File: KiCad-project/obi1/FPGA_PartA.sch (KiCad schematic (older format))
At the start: 14 parts, among them SW1 SW_Push, U3 XC6SLX16-FTG256, U4 OSC

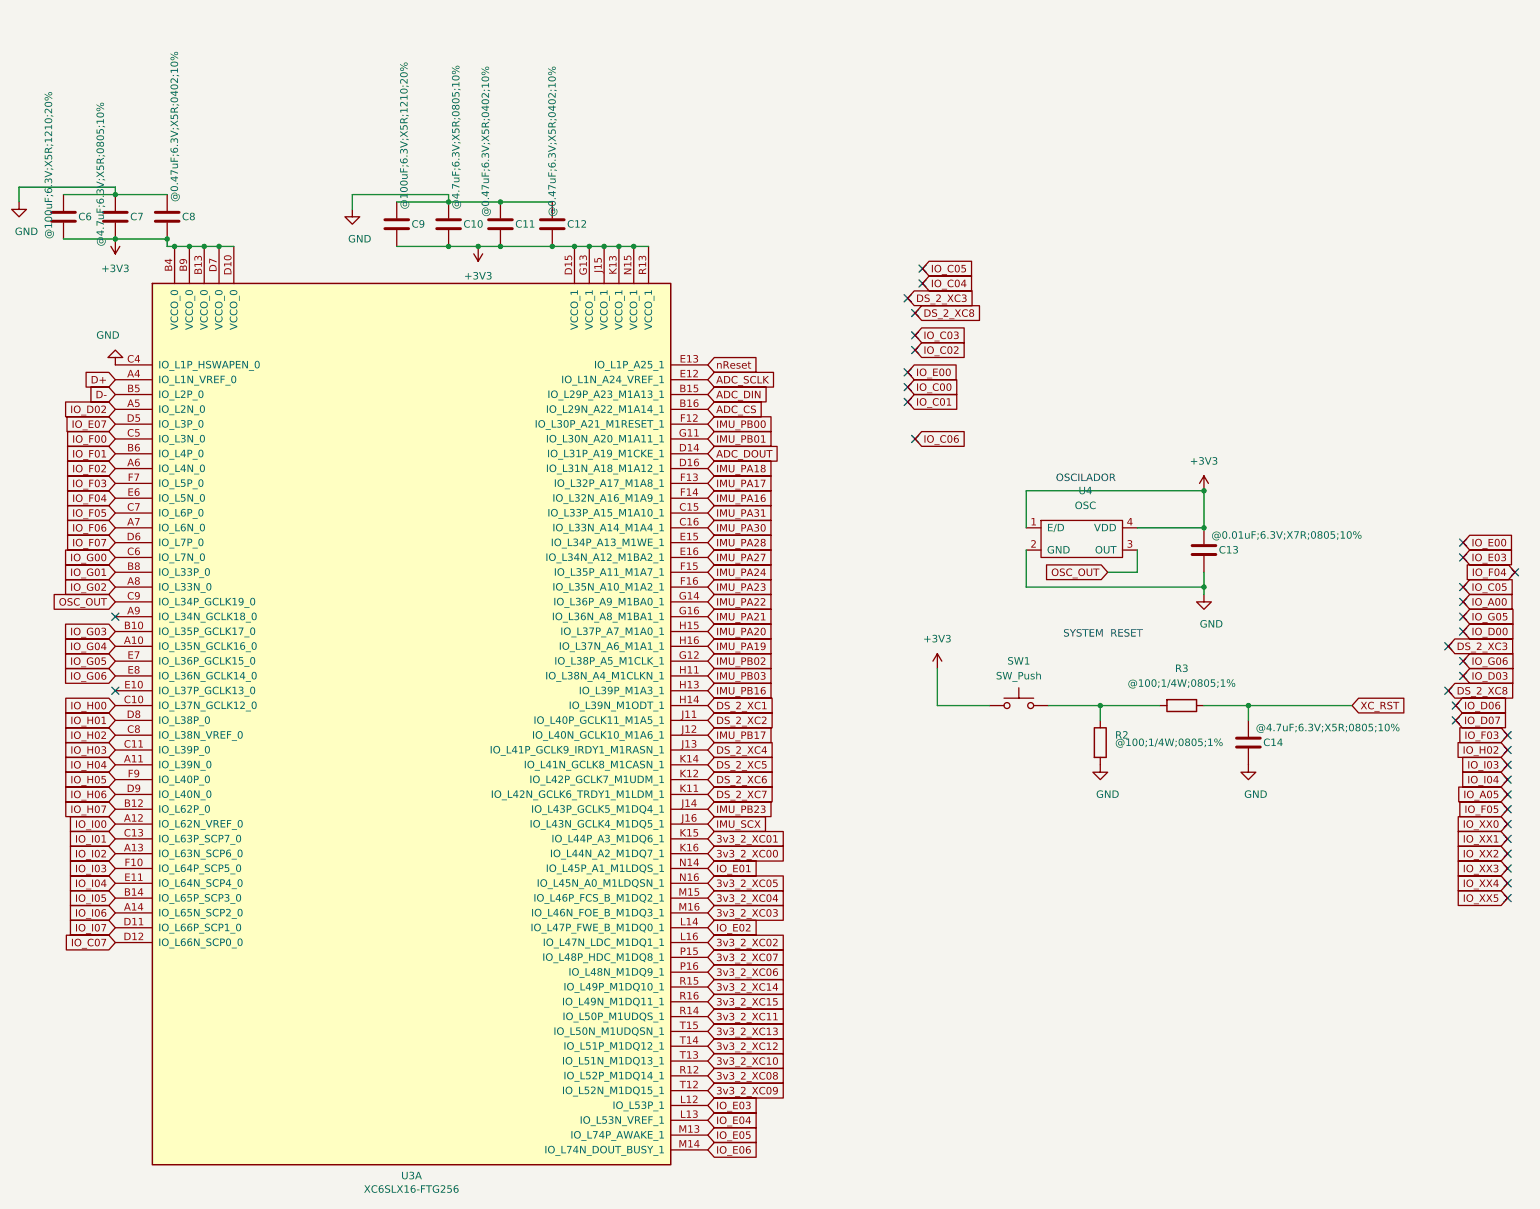
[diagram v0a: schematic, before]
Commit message: Resize board, change layout, re-route IO pins, new imu added
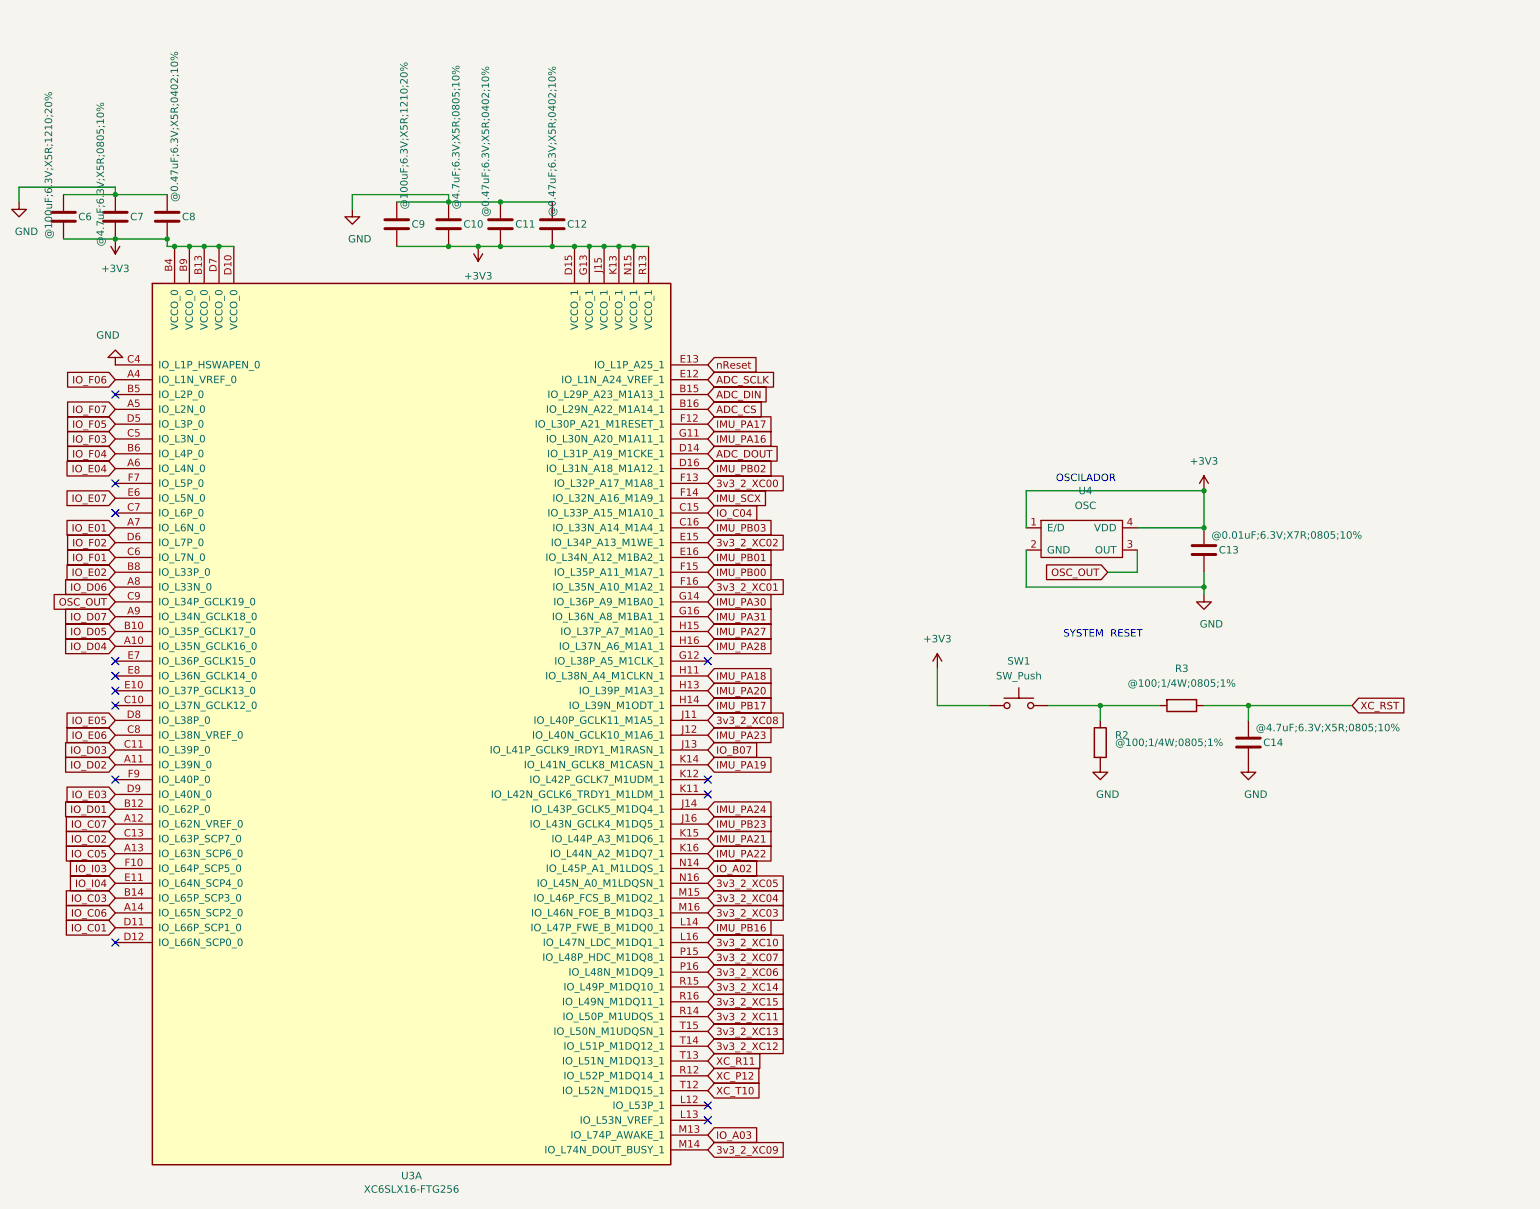
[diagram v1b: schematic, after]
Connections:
- net D+ is gone; now on net IO_F06: U3.A4 (IO_L1N_VREF_0)
- net DS_2_XC1 is gone; now on net IMU_PB17: U3.H14 (IO_L39N_M1ODT_1)
- net DS_2_XC2 is gone; now on net 3v3_2_XC08: U3.J11 (IO_L40P_GCLK11_M1A5_1)
- net DS_2_XC5 is gone; now on net IMU_PA19: U3.K14 (IO_L41N_GCLK8_M1CASN_1)
- net IO_F00 is gone; now on net IO_F03: U3.C5 (IO_L3N_0)
- net IO_G00 is gone; now on net IO_F01: U3.C6 (IO_L7N_0)
- net IO_G01 is gone; now on net IO_E02: U3.B8 (IO_L33P_0)
- net IO_G02 is gone; now on net IO_D06: U3.A8 (IO_L33N_0)
- net IO_H01 is gone; now on net IO_E05: U3.D8 (IO_L38P_0)
- net IO_H02 is gone; now on net IO_E06: U3.C8 (IO_L38N_VREF_0)
- net IO_H03 is gone; now on net IO_D03: U3.C11 (IO_L39P_0)
- net IO_H04 is gone; now on net IO_D02: U3.A11 (IO_L39N_0)
- net IO_H06 is gone; now on net IO_E03: U3.D9 (IO_L40N_0)
- net IO_I00 is gone; now on net IO_C07: U3.A12 (IO_L62N_VREF_0)
- net IO_I01 is gone; now on net IO_C02: U3.C13 (IO_L63P_SCP7_0)
- net IO_I02 is gone; now on net IO_C05: U3.A13 (IO_L63N_SCP6_0)
- net IO_I05 is gone; now on net IO_C03: U3.B14 (IO_L65P_SCP3_0)
- net IO_I06 is gone; now on net IO_C06: U3.A14 (IO_L65N_SCP2_0)
- net IO_I07 is gone; now on net IO_C01: U3.D11 (IO_L66P_SCP1_0)
- net 3v3_2_XC00: now also U3.F13 (IO_L32P_A17_M1A8_1); no longer U3.K16 (IO_L44N_A2_M1DQ7_1)
- net 3v3_2_XC01: now also U3.F16 (IO_L35N_A10_M1A2_1); no longer U3.K15 (IO_L44P_A3_M1DQ6_1)
- net 3v3_2_XC02: now also U3.E15 (IO_L34P_A13_M1WE_1); no longer U3.L16 (IO_L47N_LDC_M1DQ1_1)
- net 3v3_2_XC08: no longer U3.R12 (IO_L52P_M1DQ14_1)
- net 3v3_2_XC09: now also U3.M14 (IO_L74N_DOUT_BUSY_1); no longer U3.T12 (IO_L52N_M1DQ15_1)
- net 3v3_2_XC10: now also U3.L16 (IO_L47N_LDC_M1DQ1_1); no longer U3.T13 (IO_L51N_M1DQ13_1)
- net IMU_PA16: now also U3.G11 (IO_L30N_A20_M1A11_1); no longer U3.F14 (IO_L32N_A16_M1A9_1)
- net IMU_PA17: now also U3.F12 (IO_L30P_A21_M1RESET_1); no longer U3.F13 (IO_L32P_A17_M1A8_1)
- net IMU_PA18: now also U3.H11 (IO_L38N_A4_M1CLKN_1); no longer U3.D16 (IO_L31N_A18_M1A12_1)
- net IMU_PA19: no longer U3.H16 (IO_L37N_A6_M1A1_1)
- net IMU_PA20: now also U3.H13 (IO_L39P_M1A3_1); no longer U3.H15 (IO_L37P_A7_M1A0_1)
- net IMU_PA21: now also U3.K15 (IO_L44P_A3_M1DQ6_1); no longer U3.G16 (IO_L36N_A8_M1BA1_1)
- net IMU_PA22: now also U3.K16 (IO_L44N_A2_M1DQ7_1); no longer U3.G14 (IO_L36P_A9_M1BA0_1)
- net IMU_PA23: now also U3.J12 (IO_L40N_GCLK10_M1A6_1); no longer U3.F16 (IO_L35N_A10_M1A2_1)
- net IMU_PA24: now also U3.J14 (IO_L43P_GCLK5_M1DQ4_1); no longer U3.F15 (IO_L35P_A11_M1A7_1)
- net IMU_PA27: now also U3.H15 (IO_L37P_A7_M1A0_1); no longer U3.E16 (IO_L34N_A12_M1BA2_1)
- net IMU_PA28: now also U3.H16 (IO_L37N_A6_M1A1_1); no longer U3.E15 (IO_L34P_A13_M1WE_1)
- net IMU_PA30: now also U3.G14 (IO_L36P_A9_M1BA0_1); no longer U3.C16 (IO_L33N_A14_M1A4_1)
- net IMU_PA31: now also U3.G16 (IO_L36N_A8_M1BA1_1); no longer U3.C15 (IO_L33P_A15_M1A10_1)
- net IMU_PB00: now also U3.F15 (IO_L35P_A11_M1A7_1); no longer U3.F12 (IO_L30P_A21_M1RESET_1)
- net IMU_PB01: now also U3.E16 (IO_L34N_A12_M1BA2_1); no longer U3.G11 (IO_L30N_A20_M1A11_1)
- net IMU_PB02: now also U3.D16 (IO_L31N_A18_M1A12_1); no longer U3.G12 (IO_L38P_A5_M1CLK_1)
- net IMU_PB03: now also U3.C16 (IO_L33N_A14_M1A4_1); no longer U3.H11 (IO_L38N_A4_M1CLKN_1)
- net IMU_PB16: now also U3.L14 (IO_L47P_FWE_B_M1DQ0_1); no longer U3.H13 (IO_L39P_M1A3_1)
- net IMU_PB17: no longer U3.J12 (IO_L40N_GCLK10_M1A6_1)
- net IMU_PB23: now also U3.J16 (IO_L43N_GCLK4_M1DQ5_1); no longer U3.J14 (IO_L43P_GCLK5_M1DQ4_1)
- net IMU_SCX: now also U3.F14 (IO_L32N_A16_M1A9_1); no longer U3.J16 (IO_L43N_GCLK4_M1DQ5_1)
- net IO_C04: now also U3.C15 (IO_L33P_A15_M1A10_1)
- net IO_C07: no longer U3.D12 (IO_L66N_SCP0_0)
- net IO_D02: no longer U3.A5 (IO_L2N_0)
- net IO_D07: now also U3.A9 (IO_L34N_GCLK18_0)
- net IO_E01: now also U3.A7 (IO_L6N_0); no longer U3.N14 (IO_L45P_A1_M1LDQS_1)
- net IO_E02: no longer U3.L14 (IO_L47P_FWE_B_M1DQ0_1)
- net IO_E03: no longer U3.L12 (IO_L53P_1)
- net IO_E04: now also U3.A6 (IO_L4N_0); no longer U3.L13 (IO_L53N_VREF_1)
- net IO_E05: no longer U3.M13 (IO_L74P_AWAKE_1)
- net IO_E06: no longer U3.M14 (IO_L74N_DOUT_BUSY_1)
- net IO_E07: now also U3.E6 (IO_L5N_0); no longer U3.D5 (IO_L3P_0)
- net IO_F01: no longer U3.B6 (IO_L4P_0)
- net IO_F02: now also U3.D6 (IO_L7P_0); no longer U3.A6 (IO_L4N_0)
- net IO_F03: no longer U3.F7 (IO_L5P_0)
- net IO_F04: now also U3.B6 (IO_L4P_0); no longer U3.E6 (IO_L5N_0)
- net IO_F05: now also U3.D5 (IO_L3P_0); no longer U3.C7 (IO_L6P_0)
- net IO_F06: no longer U3.A7 (IO_L6N_0)
- net IO_F07: now also U3.A5 (IO_L2N_0); no longer U3.D6 (IO_L7P_0)
- net D-: no longer names the net of U3.B5 (IO_L2P_0)
- net DS_2_XC4 renamed IO_B07
- net DS_2_XC6: no longer names the net of U3.K12 (IO_L42P_GCLK7_M1UDM_1)
- net DS_2_XC7: no longer names the net of U3.K11 (IO_L42N_GCLK6_TRDY1_M1LDM_1)
- net IO_G03 renamed IO_D05
- net IO_G04 renamed IO_D04
- net IO_G05: no longer names the net of U3.E7 (IO_L36P_GCLK15_0)
- net IO_G06: no longer names the net of U3.E8 (IO_L36N_GCLK14_0)
- net IO_H00: no longer names the net of U3.C10 (IO_L37N_GCLK12_0)
- net IO_H05: no longer names the net of U3.F9 (IO_L40P_0)
- net IO_H07 renamed IO_D01
- new net IO_A02: U3.N14 (IO_L45P_A1_M1LDQS_1)
- new net IO_A03: U3.M13 (IO_L74P_AWAKE_1)
- new net XC_P12: U3.R12 (IO_L52P_M1DQ14_1)
- new net XC_R11: U3.T13 (IO_L51N_M1DQ13_1)
- new net XC_T10: U3.T12 (IO_L52N_M1DQ15_1)
- no-connect marks 37 -> 14

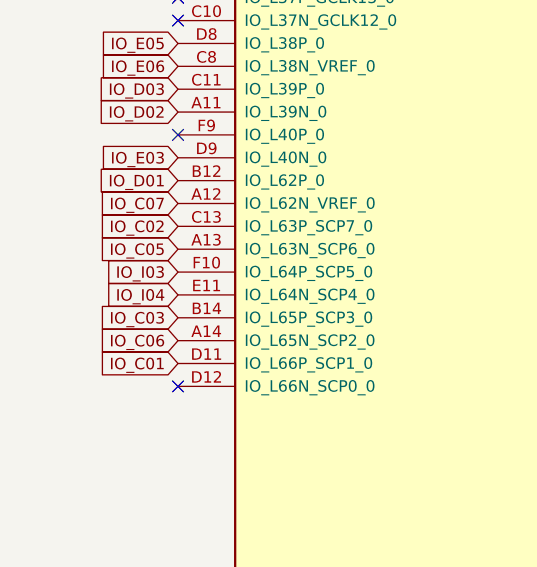
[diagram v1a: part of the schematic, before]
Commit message: Text in  Silk layer adjusted
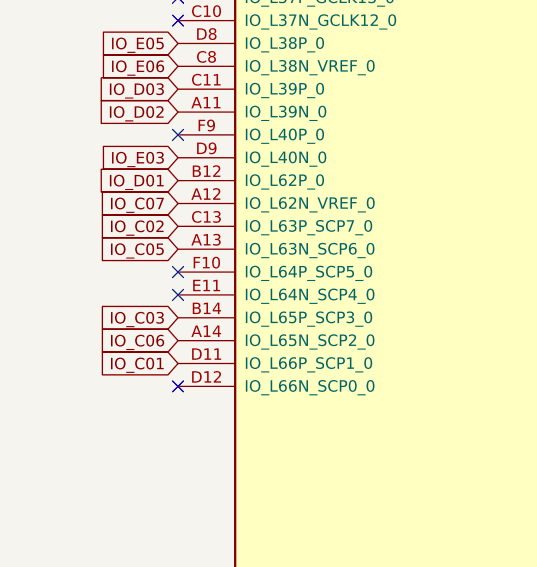
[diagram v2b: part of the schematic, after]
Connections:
- net IO_I03: no longer names the net of U3.F10 (IO_L64P_SCP5_0)
- net IO_I04: no longer names the net of U3.E11 (IO_L64N_SCP4_0)
- no-connect marks 14 -> 16
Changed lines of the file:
@@
 $Descr A4 11693 8268
 encoding utf-8
-Sheet 2 10
-Title ""
-Date ""
-Rev ""
-Comp ""
-Comment1 ""
-Comment2 ""
+Sheet 2 11
+Title "Spartan6 FTG256 Part A"
+Date "2021-04-08"
+Rev "0.2 "
+Comp "QRoboticsLab"
+Comment1 "by EGU"
+Comment2 "by JKGR"
 Comment3 ""
 Comment4 ""
@@
 	9900 4000 9200 4000
 Connection ~ 9200 4000
-Text GLabel 1550 5100 0    50   Input ~ 0
-IO_I03
-Text GLabel 1550 5200 0    50   Input ~ 0
-IO_I04
 NoConn ~ 1550 3900
 Text GLabel 5550 3100 2    50   Input ~ 0
@@
 NoConn ~ 1550 3800
 NoConn ~ 1550 3700
+NoConn ~ 1550 5100
+NoConn ~ 1550 5200
 $EndSCHEMATC

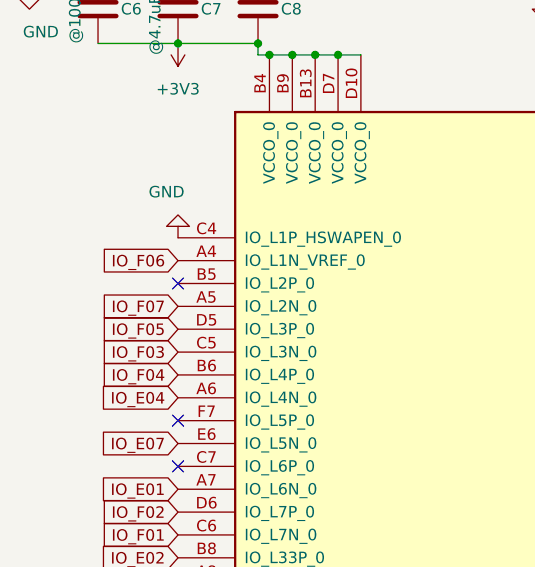
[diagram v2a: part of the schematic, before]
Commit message: Changed RAM by Cypres Model -rebuild symbolic and changed footprint
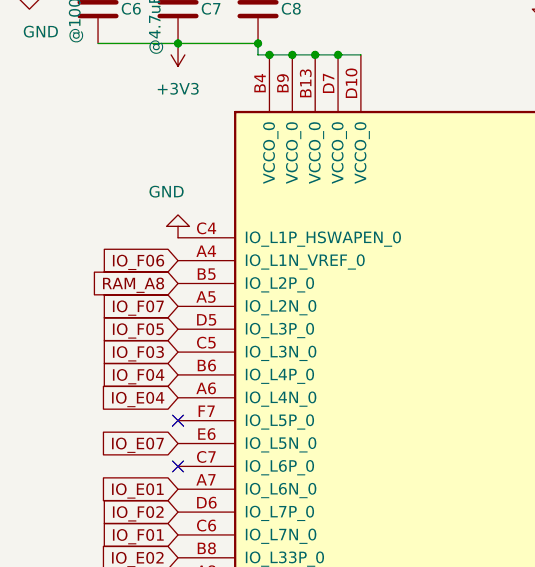
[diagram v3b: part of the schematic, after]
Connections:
- net RAM_A8: now reaches U3.B5 (IO_L2P_0)
- no-connect marks 16 -> 15
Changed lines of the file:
@@
 NoConn ~ 5550 4600
 NoConn ~ 5550 3700
-NoConn ~ 1550 1900
 NoConn ~ 1550 2500
 NoConn ~ 1550 2700
@@
 NoConn ~ 1550 5100
 NoConn ~ 1550 5200
+Text GLabel 1550 1900 0    50   Input ~ 0
+RAM_A8
 $EndSCHEMATC
